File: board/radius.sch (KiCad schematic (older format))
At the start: 6 parts

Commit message: Commit #2
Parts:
- added C1: C, Capacitors_SMD:C_0603_HandSoldering, symbol C
- added P1: CONN_01X04, Socket_Strips:Socket_Strip_Straight_1x04, symbol CONN_01X04
- added P2: CONN_01X10, Socket_Strips:Socket_Strip_Angled_1x10, symbol CONN_01X10
- added U1: CH340G, Housings_SSOP:SSOP-16_3.9x4.9mm_Pitch0.635mm, symbol CH340G
- added U2: LM2931AZ-3.3/5.0, Power_Integrations:SO-8, symbol LM2931AZ-3.3/5.0
- C2, C3, C4, C5: renamed from C?; footprint (none) -> Capacitors_SMD:C_0603_HandSoldering
- IC1: renamed from IC?; footprint TSSOP-20 -> Housings_SSOP:TSSOP-20_4.4x6.5mm_Pitch0.65mm
- Y1: renamed from Y?; footprint (none) -> Crystals:Crystal_SMD_0603_4Pads
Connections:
- net GND: now also C1.2, P1.4 (P4), P2.1 (P1), U1.1 (GND), U2.2 (GND)
- net SDA: now reaches IC1.11 ([TIM1_BKIN]I2C_SDA/PB5)
- net SDA: now also P2.3 (P3)
- net SCL: now reaches IC1.12 ([ADC_ETR]I2C_SCL/PB4)
- net SCL: now also P2.4 (P4)
- net SCK: now reaches IC1.15 ([TIM2_CH1]SPI_SCK/PC5)
- net SCK: now also P2.5 (P5)
- net MOSI: now reaches IC1.16 ([TIM1_CH1]SPI_MOSI/PC6)
- net MOSI: now also P2.7 (P7)
- net MISO: now reaches IC1.17 ([TIM1_CH2]SPI_MISO/PC7)
- net MISO: now also P2.6 (P6)
- net G3: now reaches IC1.18 (PD1/SWIM)
- net G3: now also P2.10 (P10)
- net TXD: now reaches IC1.19 (PD2/AIN3[TIM2_CH3])
- net TXD: now also P2.8 (P8)
- net USB_TX: now reaches IC1.2 (PD5/AIN5/UART1_TX)
- net USB_TX: now also U1.2 (TXD)
- net RXD: now reaches IC1.20 (PD3/AIN4/TIM2_CH2)
- net RXD: now also P2.9 (P9)
- net USB_RX: now reaches IC1.3 (PD6/AIN6/UART1_RX)
- net USB_RX: now also U1.3 (RXD)
- net XO: now reaches C4.2, IC1.5 (OSCIN/PA1), Y1.1
- net XO: now also U1.8 (XO)
- net XI: now reaches C5.2, IC1.6 (OSCOUT/PA2), Y1.2
- net XI: now also U1.7 (XI)
- net VDD renamed VCC
- net VCC: now also P2.2 (P2), U1.16 (VCC), U2.1 (VO)
- new net: C1.1, U1.4 (V3)
- new net +5V: P1.1 (P1), U2.3 (VI)
- new net D+: P1.2 (P2), U1.5 (UD+)
- new net D-: P1.3 (P3), U1.6 (UD-)
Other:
- moved on the sheet: C4, C5, Y1

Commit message: Qualifying layout
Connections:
- net G3: now also IC1.14 ([TIM1_CH2N]AIN2/TIM1_CH4/PC4); no longer IC1.18 (PD1/SWIM)
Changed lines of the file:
@@
 $EndComp
 $Comp
-L GND #PWR5
+L GND #PWR01
 U 1 1 557FA54B
 P 4100 3900
-F 0 "#PWR5" H 4100 3650 50  0001 C CNN
+F 0 "#PWR01" H 4100 3650 50  0001 C CNN
 F 1 "GND" H 4100 3750 50  0000 C CNN
 F 2 "" H 4100 3900 60  0000 C CNN
@@
 $EndComp
 $Comp
-L GND #PWR9
+L GND #PWR02
 U 1 1 557FB0DB
 P 6000 3900
-F 0 "#PWR9" H 6000 3650 50  0001 C CNN
+F 0 "#PWR02" H 6000 3650 50  0001 C CNN
 F 1 "GND" H 6000 3750 50  0000 C CNN
 F 2 "" H 6000 3900 60  0000 C CNN
@@
 $EndComp
 $Comp
-L GND #PWR3
+L GND #PWR03
 U 1 1 557FB357
 P 2700 2400
-F 0 "#PWR3" H 2700 2150 50  0001 C CNN
+F 0 "#PWR03" H 2700 2150 50  0001 C CNN
 F 1 "GND" H 2700 2250 50  0000 C CNN
 F 2 "" H 2700 2400 60  0000 C CNN
@@
 $EndComp
 $Comp
-L GND #PWR15
+L GND #PWR04
 U 1 1 557FB5FD
 P 10250 1000
-F 0 "#PWR15" H 10250 750 50  0001 C CNN
+F 0 "#PWR04" H 10250 750 50  0001 C CNN
 F 1 "GND" H 10250 850 50  0000 C CNN
 F 2 "" H 10250 1000 60  0000 C CNN
@@
 $EndComp
 $Comp
-L GND #PWR16
+L GND #PWR05
 U 1 1 557FB61D
 P 10250 1650
-F 0 "#PWR16" H 10250 1400 50  0001 C CNN
+F 0 "#PWR05" H 10250 1400 50  0001 C CNN
 F 1 "GND" H 10250 1500 50  0000 C CNN
 F 2 "" H 10250 1650 60  0000 C CNN
@@
 Text GLabel 3600 3050 0    60   Output ~ 0
 USB_RX
-Text GLabel 3800 2500 0    60   Output ~ 0
+Text GLabel 7800 3050 2    60   Output ~ 0
 G3
 Text GLabel 3800 2650 0    60   Output ~ 0
@@
 $EndComp
 $Comp
-L GND #PWR7
+L GND #PWR06
 U 1 1 557FBE42
 P 5200 6250
-F 0 "#PWR7" H 5200 6000 50  0001 C CNN
+F 0 "#PWR06" H 5200 6000 50  0001 C CNN
 F 1 "GND" H 5200 6100 50  0000 C CNN
 F 2 "" H 5200 6250 60  0000 C CNN
@@
 $EndComp
 $Comp
-L VCC #PWR6
+L VCC #PWR07
 U 1 1 557FBEB7
 P 5200 4800
-F 0 "#PWR6" H 5200 4650 50  0001 C CNN
+F 0 "#PWR07" H 5200 4650 50  0001 C CNN
 F 1 "VCC" H 5200 4950 50  0000 C CNN
 F 2 "" H 5200 4800 60  0000 C CNN
@@
 $EndComp
 $Comp
-L GND #PWR4
+L GND #PWR08
 U 1 1 557FC04A
 P 2750 6300
-F 0 "#PWR4" H 2750 6050 50  0001 C CNN
+F 0 "#PWR08" H 2750 6050 50  0001 C CNN
 F 1 "GND" H 2750 6150 50  0000 C CNN
 F 2 "" H 2750 6300 60  0000 C CNN
@@
 Wire Wire Line
 	4200 2650 3800 2650
-Wire Wire Line
-	3800 2500 4700 2500
 Wire Wire Line
 	4700 6100 5200 6100
@@
 $EndComp
 $Comp
-L VCC #PWR8
+L VCC #PWR09
 U 1 1 557FCD3A
 P 6000 1600
-F 0 "#PWR8" H 6000 1450 50  0001 C CNN
+F 0 "#PWR09" H 6000 1450 50  0001 C CNN
 F 1 "VCC" H 6000 1750 50  0000 C CNN
 F 2 "" H 6000 1600 60  0000 C CNN
@@
 $EndComp
 $Comp
-L +5V #PWR10
+L +5V #PWR010
 U 1 1 557FCD60
 P 7400 4900
-F 0 "#PWR10" H 7400 4750 50  0001 C CNN
+F 0 "#PWR010" H 7400 4750 50  0001 C CNN
 F 1 "+5V" H 7400 5040 50  0000 C CNN
 F 2 "" H 7400 4900 60  0000 C CNN
@@
 $EndComp
 $Comp
-L VCC #PWR12
+L VCC #PWR011
 U 1 1 557FCD86
 P 9000 4900
-F 0 "#PWR12" H 9000 4750 50  0001 C CNN
+F 0 "#PWR011" H 9000 4750 50  0001 C CNN
 F 1 "VCC" H 9000 5050 50  0000 C CNN
 F 2 "" H 9000 4900 60  0000 C CNN
@@
 $EndComp
 $Comp
-L GND #PWR11
+L GND #PWR012
 U 1 1 557FCDAC
 P 8150 5400
-F 0 "#PWR11" H 8150 5150 50  0001 C CNN
+F 0 "#PWR012" H 8150 5150 50  0001 C CNN
 F 1 "GND" H 8150 5250 50  0000 C CNN
 F 2 "" H 8150 5400 60  0000 C CNN
@@
 D-
 $Comp
-L GND #PWR14
+L GND #PWR013
 U 1 1 557FD427
 P 9200 4200
-F 0 "#PWR14" H 9200 3950 50  0001 C CNN
+F 0 "#PWR013" H 9200 3950 50  0001 C CNN
 F 1 "GND" H 9200 4050 50  0000 C CNN
 F 2 "" H 9200 4200 60  0000 C CNN
@@
 $EndComp
 $Comp
-L +5V #PWR13
+L +5V #PWR014
 U 1 1 557FD44F
 P 9200 3450
-F 0 "#PWR13" H 9200 3300 50  0001 C CNN
+F 0 "#PWR014" H 9200 3300 50  0001 C CNN
 F 1 "+5V" H 9200 3590 50  0000 C CNN
 F 2 "" H 9200 3450 60  0000 C CNN
@@
 $EndComp
 $Comp
-L GND #PWR2
+L GND #PWR015
 U 1 1 557FD669
 P 1400 5400
-F 0 "#PWR2" H 1400 5150 50  0001 C CNN
+F 0 "#PWR015" H 1400 5150 50  0001 C CNN
 F 1 "GND" H 1400 5250 50  0000 C CNN
 F 2 "" H 1400 5400 60  0000 C CNN
@@
 $EndComp
 $Comp
-L VCC #PWR1
+L VCC #PWR016
 U 1 1 557FD693
 P 1350 4000
-F 0 "#PWR1" H 1350 3850 50  0001 C CNN
+F 0 "#PWR016" H 1350 3850 50  0001 C CNN
 F 1 "VCC" H 1350 4150 50  0000 C CNN
 F 2 "" H 1350 4000 60  0000 C CNN
@@
 Wire Wire Line
 	1000 5400 1400 5400
+Wire Wire Line
+	7800 3050 7300 3050
+Wire Wire Line
+	7300 3050 7300 3000
 $EndSCHEMATC

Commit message: Adds missing capacitor on regulator.
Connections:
- net VCC: now also C1.1
- net at C2.1, IC1.4 (NRST): now also U1.4 (V3)
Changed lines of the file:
@@
-	1    0    0    -1
-$EndComp
-$Comp
-L C C1
-U 1 1 557FBFD1
-P 2750 6050
-F 0 "C1" H 2775 6150 50  0000 L CNN
-F 1 "C" H 2775 5950 50  0000 L CNN
-F 2 "Capacitors_SMD:C_0603_HandSoldering" H 2788 5900 30  0001 C CNN
-F 3 "" H 2750 6050 60  0000 C CNN
-	1    2750 6050
-	1    0    0    -1
-$EndComp
-$Comp
-L GND #PWR08
-U 1 1 557FC04A
-P 2750 6300
-F 0 "#PWR08" H 2750 6050 50  0001 C CNN
-F 1 "GND" H 2750 6150 50  0000 C CNN
-F 2 "" H 2750 6300 60  0000 C CNN
-F 3 "" H 2750 6300 60  0000 C CNN
-	1    2750 6300
 	1    0    0    -1
 $EndComp
@@
 	5200 5000 5200 4800
 Wire Wire Line
-	3700 5800 2750 5800
-Wire Wire Line
-	2750 5800 2750 5900
-Wire Wire Line
-	2750 6200 2750 6300
+	2750 5800 3700 5800
+Wire Wire Line
+	2750 2650 2750 5800
 Wire Wire Line
 	4700 5200 5550 5200
@@
 $EndComp
 $Comp
-L VCC #PWR09
+L VCC #PWR08
 U 1 1 557FCD3A
 P 6000 1600
-F 0 "#PWR09" H 6000 1450 50  0001 C CNN
+F 0 "#PWR08" H 6000 1450 50  0001 C CNN
 F 1 "VCC" H 6000 1750 50  0000 C CNN
 F 2 "" H 6000 1600 60  0000 C CNN
@@
 $EndComp
 $Comp
-L +5V #PWR010
+L +5V #PWR09
 U 1 1 557FCD60
 P 7400 4900
-F 0 "#PWR010" H 7400 4750 50  0001 C CNN
+F 0 "#PWR09" H 7400 4750 50  0001 C CNN
 F 1 "+5V" H 7400 5040 50  0000 C CNN
 F 2 "" H 7400 4900 60  0000 C CNN
@@
 $EndComp
 $Comp
-L VCC #PWR011
+L VCC #PWR010
 U 1 1 557FCD86
 P 9000 4900
-F 0 "#PWR011" H 9000 4750 50  0001 C CNN
+F 0 "#PWR010" H 9000 4750 50  0001 C CNN
 F 1 "VCC" H 9000 5050 50  0000 C CNN
 F 2 "" H 9000 4900 60  0000 C CNN
@@
 $EndComp
 $Comp
-L GND #PWR012
+L GND #PWR011
 U 1 1 557FCDAC
 P 8150 5400
-F 0 "#PWR012" H 8150 5150 50  0001 C CNN
+F 0 "#PWR011" H 8150 5150 50  0001 C CNN
 F 1 "GND" H 8150 5250 50  0000 C CNN
 F 2 "" H 8150 5400 60  0000 C CNN
@@
 D-
 $Comp
-L GND #PWR013
+L GND #PWR012
 U 1 1 557FD427
 P 9200 4200
-F 0 "#PWR013" H 9200 3950 50  0001 C CNN
+F 0 "#PWR012" H 9200 3950 50  0001 C CNN
 F 1 "GND" H 9200 4050 50  0000 C CNN
 F 2 "" H 9200 4200 60  0000 C CNN
@@
 $EndComp
 $Comp
-L +5V #PWR014
+L +5V #PWR013
 U 1 1 557FD44F
 P 9200 3450
-F 0 "#PWR014" H 9200 3300 50  0001 C CNN
+F 0 "#PWR013" H 9200 3300 50  0001 C CNN
 F 1 "+5V" H 9200 3590 50  0000 C CNN
 F 2 "" H 9200 3450 60  0000 C CNN
@@
 $EndComp
 $Comp
-L GND #PWR015
+L GND #PWR014
 U 1 1 557FD669
 P 1400 5400
-F 0 "#PWR015" H 1400 5150 50  0001 C CNN
+F 0 "#PWR014" H 1400 5150 50  0001 C CNN
 F 1 "GND" H 1400 5250 50  0000 C CNN
 F 2 "" H 1400 5400 60  0000 C CNN
@@
 $EndComp
 $Comp
-L VCC #PWR016
+L VCC #PWR015
 U 1 1 557FD693
 P 1350 4000
-F 0 "#PWR016" H 1350 3850 50  0001 C CNN
+F 0 "#PWR015" H 1350 3850 50  0001 C CNN
 F 1 "VCC" H 1350 4150 50  0000 C CNN
 F 2 "" H 1350 4000 60  0000 C CNN
@@
 Wire Wire Line
 	7300 3050 7300 3000
+Wire Wire Line
+	2750 2650 3350 2650
+Wire Wire Line
+	3350 2650 3350 1400
+Connection ~ 3350 1400
+$Comp
+L C C1
+U 1 1 558B5C2A
+P 8700 5150
+F 0 "C1" H 8725 5250 50  0000 L CNN
+F 1 "C" H 8725 5050 50  0000 L CNN
+F 2 "Capacitors_SMD:C_0603_HandSoldering" H 8738 5000 30  0001 C CNN
+F 3 "" H 8700 5150 60  0000 C CNN
+	1    8700 5150
+	1    0    0    -1
+$EndComp
+Wire Wire Line
+	8700 5000 8700 4900
+Connection ~ 8700 4900
+Wire Wire Line
+	8700 5300 8150 5300
+Connection ~ 8150 5300
 $EndSCHEMATC

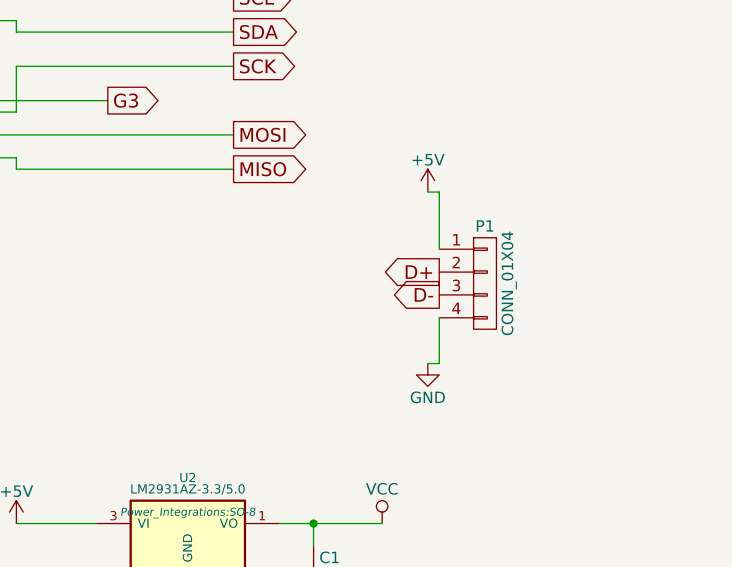
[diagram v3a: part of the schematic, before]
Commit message: Adds USB connector.
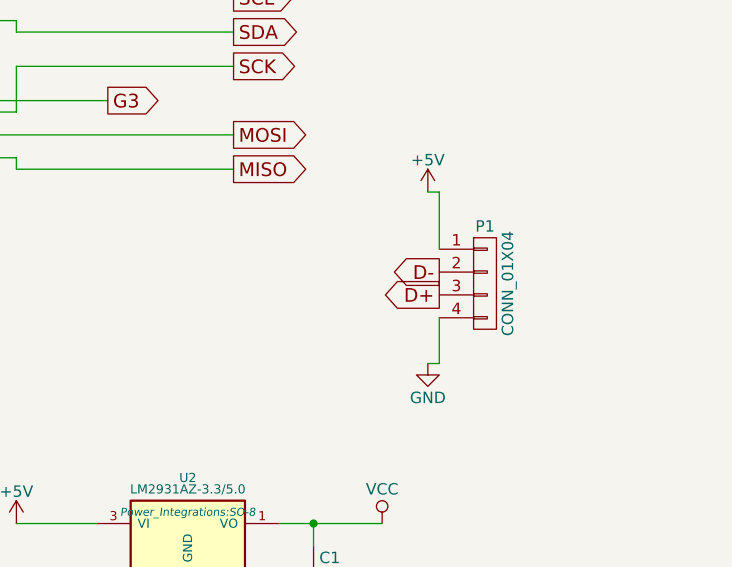
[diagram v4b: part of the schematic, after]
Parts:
- P1: footprint Socket_Strips:Socket_Strip_Straight_1x04 -> usbpcb:USB-A-PCB
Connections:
- net D+: now also P1.3 (P3); no longer P1.2 (P2)
- net D-: now also P1.2 (P2); no longer P1.3 (P3)
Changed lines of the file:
@@
 F 0 "P1" H 9450 4100 50  0000 C CNN
 F 1 "CONN_01X04" V 9550 3850 50  0000 C CNN
-F 2 "Socket_Strips:Socket_Strip_Straight_1x04" H 9450 3850 60  0001 C CNN
+F 2 "usbpcb:USB-A-PCB" H 9450 3850 60  0001 C CNN
 F 3 "" H 9450 3850 60  0000 C CNN
 	1    9450 3850
@@
 $EndComp
 Text GLabel 9250 3800 0    60   Output ~ 0
+D-
+Text GLabel 9250 3900 0    60   Output ~ 0
 D+
-Text GLabel 9250 3900 0    60   Output ~ 0
-D-
 $Comp
 L GND #PWR012

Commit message: Corrects footprints for CH340G, start over.
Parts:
- U1: footprint Housings_SSOP:SSOP-16_3.9x4.9mm_Pitch0.635mm -> SMD_Packages:SO-16-N
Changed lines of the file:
@@
 F 0 "U1" H 4200 6250 60  0000 C CNN
 F 1 "CH340G" H 4200 4850 60  0000 C CNN
-F 2 "Housings_SSOP:SSOP-16_3.9x4.9mm_Pitch0.635mm" H 4150 6650 60  0001 C CNN
+F 2 "SMD_Packages:SO-16-N" H 4150 6650 60  0001 C CNN
 F 3 "" H 4150 6650 60  0000 C CNN
 	1    4200 5550

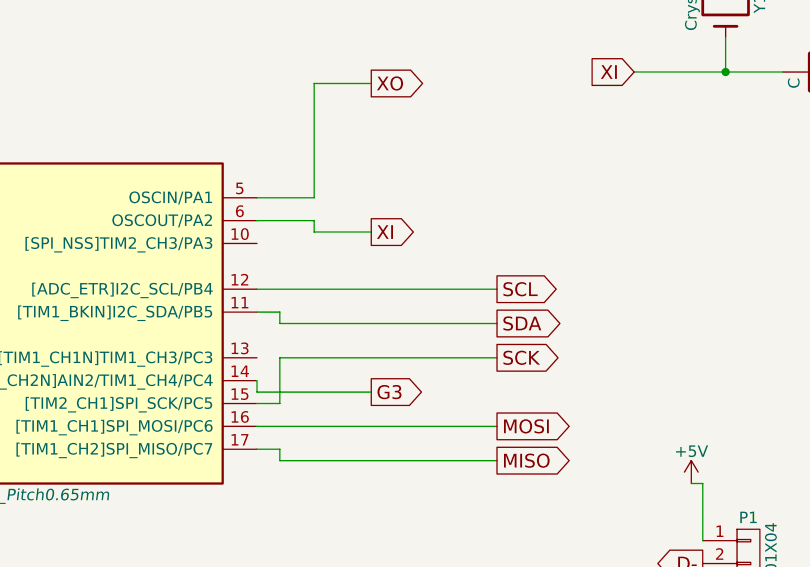
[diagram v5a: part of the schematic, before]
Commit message: Completes power rails, layout.
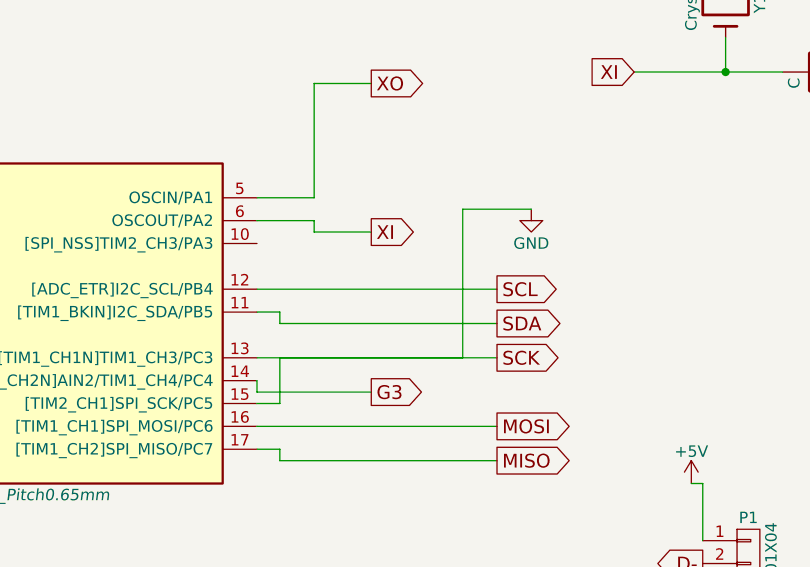
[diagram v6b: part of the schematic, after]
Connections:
- net SCK is gone; now on net GND: IC1.15 ([TIM2_CH1]SPI_SCK/PC5), P2.5 (P5)
- net GND: now also IC1.13 ([TIM1_CH1N]TIM1_CH3/PC3)
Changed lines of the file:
@@
 	8700 5300 8150 5300
 Connection ~ 8150 5300
+Wire Wire Line
+	7300 2900 8200 2900
+Wire Wire Line
+	8200 2900 8200 2250
+Wire Wire Line
+	8200 2250 8500 2250
+$Comp
+L GND #PWR?
+U 1 1 559188A2
+P 8500 2250
+F 0 "#PWR?" H 8500 2000 50  0001 C CNN
+F 1 "GND" H 8500 2100 50  0000 C CNN
+F 2 "" H 8500 2250 60  0000 C CNN
+F 3 "" H 8500 2250 60  0000 C CNN
+	1    8500 2250
+	1    0    0    -1
+$EndComp
 $EndSCHEMATC

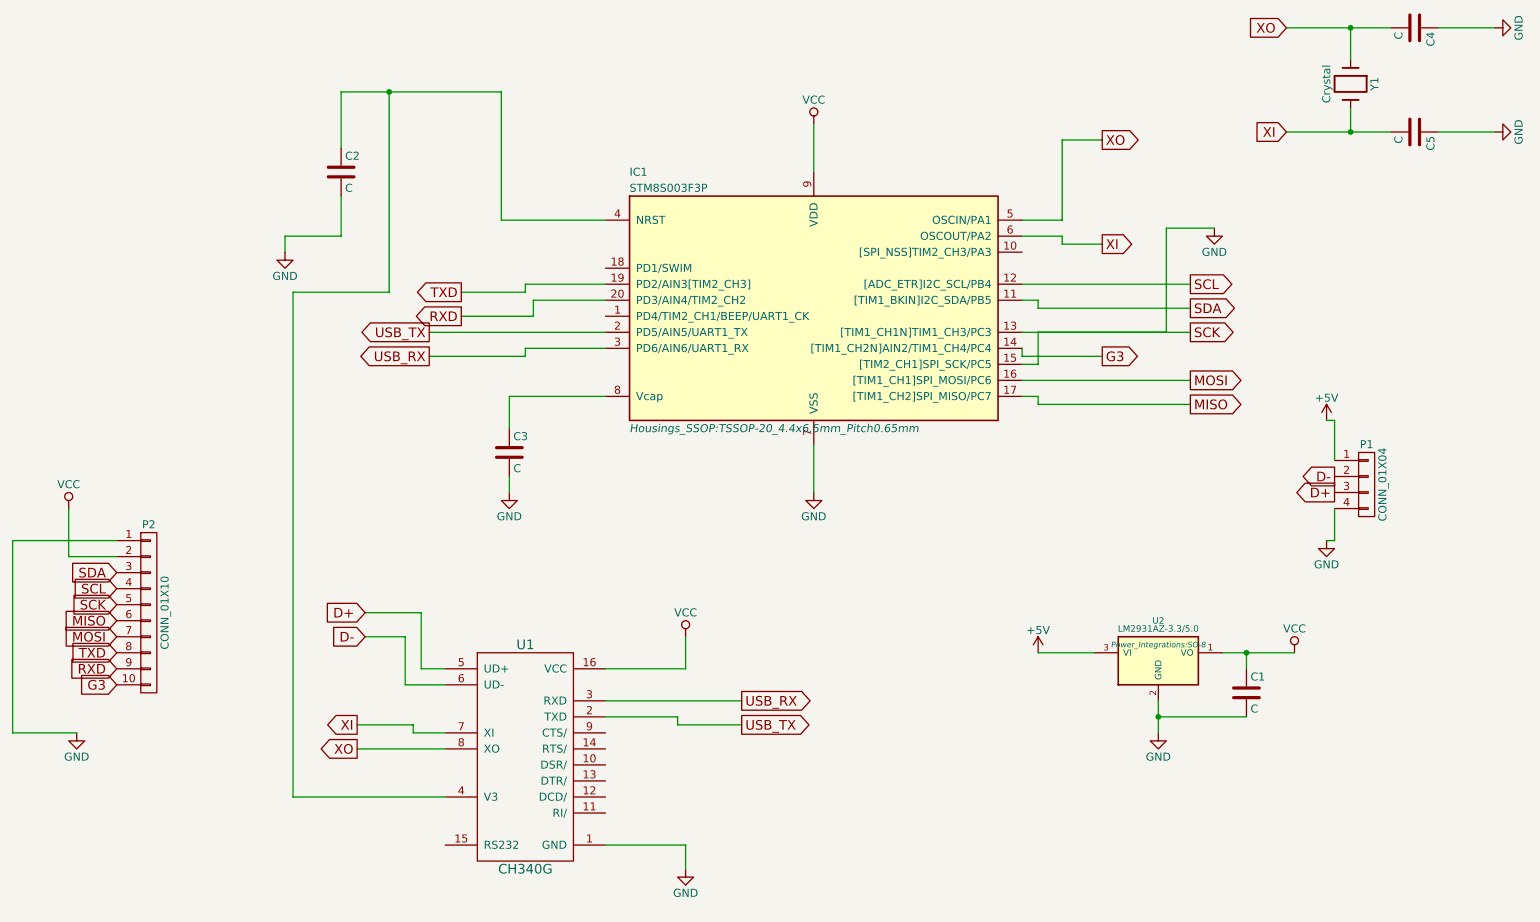
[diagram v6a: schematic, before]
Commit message: Updates Capacitor values.
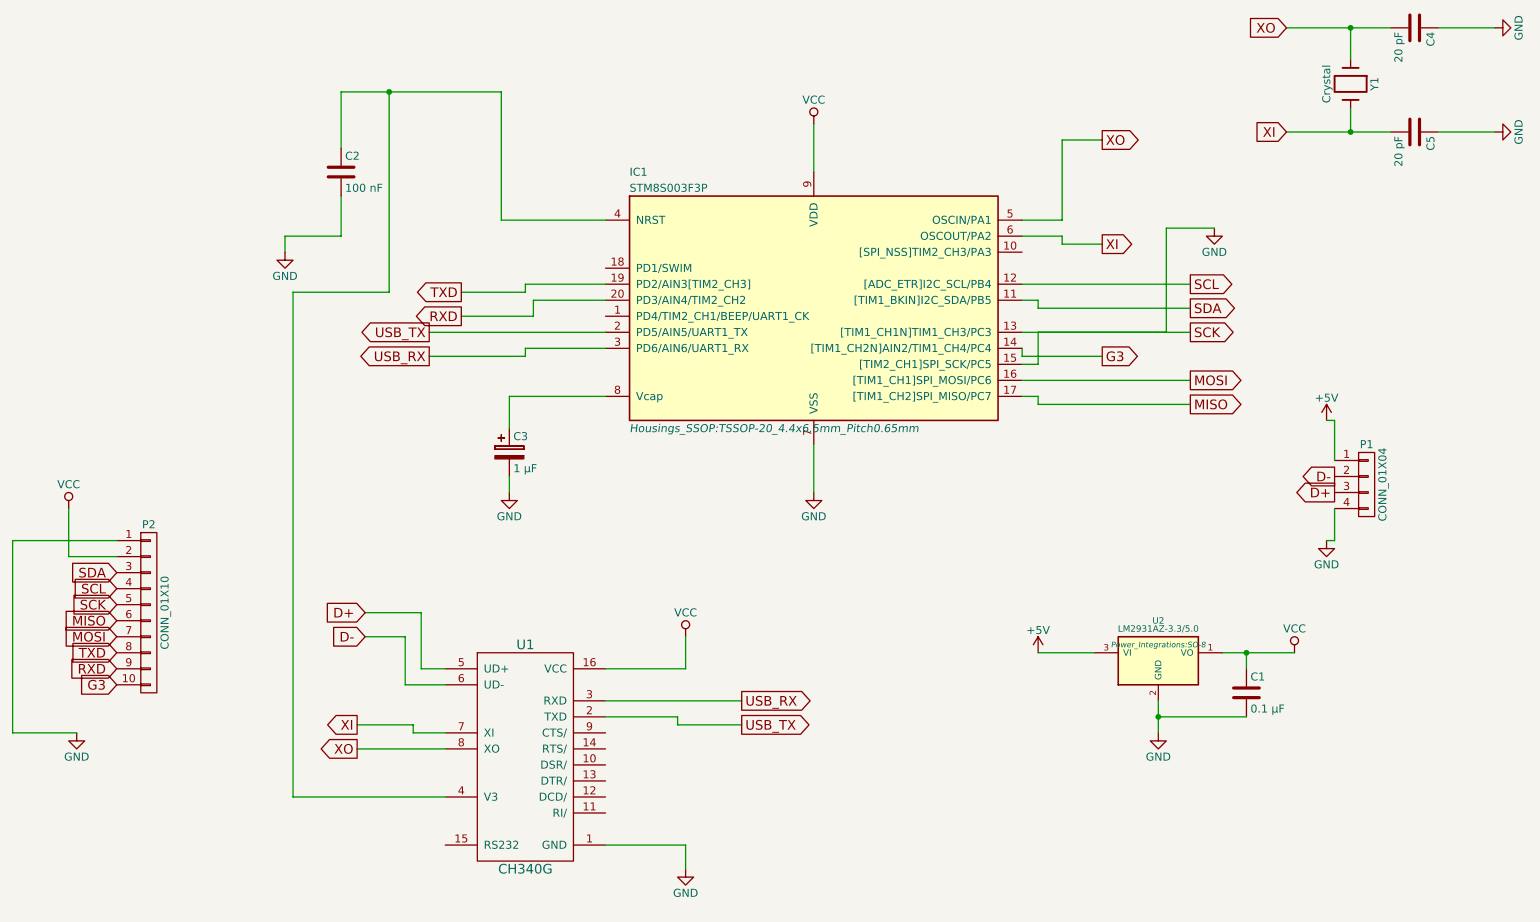
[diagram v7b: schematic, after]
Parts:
- removed C3: C, Capacitors_SMD:C_0603_HandSoldering, symbol C
- added C3: 1 μF, Capacitors_SMD:C_0603_HandSoldering, symbol CP
- C1: value C -> 0.1 µF
- C2: value C -> 100 nF
- C4, C5: value C -> 20 pF
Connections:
- net GND: now also C3.2
- net at IC1.8 (Vcap): now also C3.1
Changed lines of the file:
@@
-$EndComp
-$Comp
-L C C3
-U 1 1 557FA561
-P 4100 3650
-F 0 "C3" H 4125 3750 50  0000 L CNN
-F 1 "C" H 4125 3550 50  0000 L CNN
-F 2 "Capacitors_SMD:C_0603_HandSoldering" H 4138 3500 30  0001 C CNN
-F 3 "" H 4100 3650 60  0000 C CNN
-	1    4100 3650
-	1    0    0    -1
 $EndComp
 $Comp
@@
 P 3050 1900
 F 0 "C2" H 3075 2000 50  0000 L CNN
-F 1 "C" H 3075 1800 50  0000 L CNN
+F 1 "100 nF" H 3075 1800 50  0000 L CNN
 F 2 "Capacitors_SMD:C_0603_HandSoldering" H 3088 1750 30  0001 C CNN
 F 3 "" H 3050 1900 60  0000 C CNN
@@
 P 9750 1000
 F 0 "C4" H 9775 1100 50  0000 L CNN
-F 1 "C" H 9775 900 50  0000 L CNN
+F 1 "20 pF" H 9775 900 50  0000 L CNN
 F 2 "Capacitors_SMD:C_0603_HandSoldering" H 9788 850 30  0001 C CNN
 F 3 "" H 9750 1000 60  0000 C CNN
@@
 P 9750 1650
 F 0 "C5" H 9775 1750 50  0000 L CNN
-F 1 "C" H 9775 1550 50  0000 L CNN
+F 1 "20 pF" H 9775 1550 50  0000 L CNN
 F 2 "Capacitors_SMD:C_0603_HandSoldering" H 9788 1500 30  0001 C CNN
 F 3 "" H 9750 1650 60  0000 C CNN
@@
 P 8700 5150
 F 0 "C1" H 8725 5250 50  0000 L CNN
-F 1 "C" H 8725 5050 50  0000 L CNN
+F 1 "0.1 µF" H 8725 5050 50  0000 L CNN
 F 2 "Capacitors_SMD:C_0603_HandSoldering" H 8738 5000 30  0001 C CNN
 F 3 "" H 8700 5150 60  0000 C CNN
@@
 	8200 2250 8500 2250
 $Comp
-L GND #PWR?
+L GND #PWR016
 U 1 1 559188A2
 P 8500 2250
-F 0 "#PWR?" H 8500 2000 50  0001 C CNN
+F 0 "#PWR016" H 8500 2000 50  0001 C CNN
 F 1 "GND" H 8500 2100 50  0000 C CNN
 F 2 "" H 8500 2250 60  0000 C CNN
@@
 	1    0    0    -1
 $EndComp
+$Comp
+L CP C3
+U 1 1 5592A3F7
+P 4100 3650
+F 0 "C3" H 4125 3750 50  0000 L CNN
+F 1 "1 μF" H 4125 3550 50  0000 L CNN
+F 2 "Capacitors_SMD:C_0603_HandSoldering" H 4138 3500 30  0001 C CNN
+F 3 "" H 4100 3650 60  0000 C CNN
+	1    4100 3650
+	1    0    0    -1
+$EndComp
